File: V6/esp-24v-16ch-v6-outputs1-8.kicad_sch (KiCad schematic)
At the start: 5 parts, among them Q4 MMBT2222A

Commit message: V6 is up
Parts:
- R89: renamed from R88; Package 0402/1005 -> (none)
- R90: renamed from R89; value 1k -> 470R; LCSC Part # C11702 -> C25117; Mfr PN 0402WGF1001TCE -> 0402WGF4700TCE; Vendor PN C11702 -> C25117
- renumbered D57 to D58, R90 to R91
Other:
- note added: "I_{BASE} = (3.3V - V_{BE}) / 470R I_{BASE} = (3.3V - 0.7V) / 470R I_{BASE} = 5,53 mA ADEQUATE FOR FULL SATURATION OF THE TRANSISTOR UP TO I_{C} AROUND 550 mA CONSIDERING A FORCED BETA OF 10."

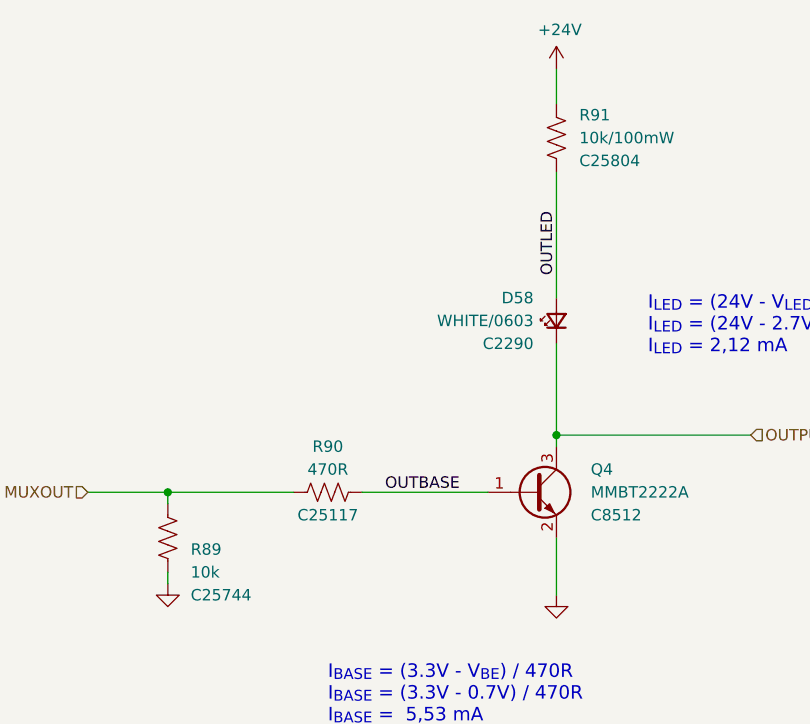
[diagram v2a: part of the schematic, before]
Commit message: Added voltage monitors for both ESP32 and LAN8710A
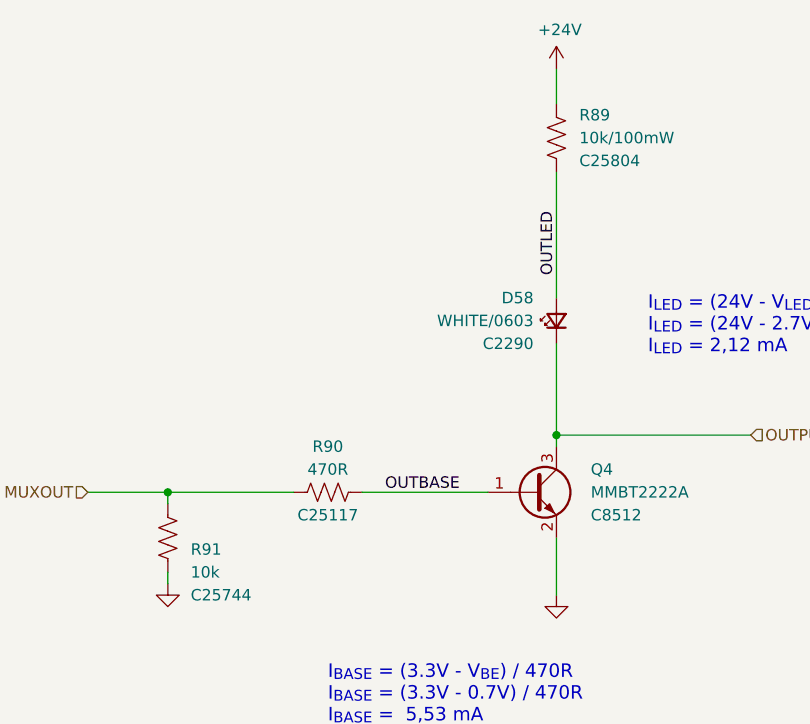
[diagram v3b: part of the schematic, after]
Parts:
- renumbered R91 to R89, R89 to R91
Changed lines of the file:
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@@
 		(title "ESP 24V 16xIn/16xOut/1-Wire Module")
 		(date "2026-02-10")
-		(rev "V6.0")
+		(rev "V6.0.3")
 	)
 	(text "I_{LED} = (24V - V_{LED} - V_{CE}) / 10k\nI_{LED} = (24V - 2.7V - 0,1V) / 10k\nI_{LED} = 2,12 mA"
@@
 		(in_pos_files yes)
 		(dnp no)
-		(property "Reference" "#PWR0217"
+		(property "Reference" "#PWR0215"
 			(at 144.78 58.42 0)
 			(hide yes)
@@
 			(project "esp-24v-16ch-v6"
 				(path "/2bc5a21a-1d79-419d-a592-6852cc07b00a/032d24f7-dea6-43c8-b36e-6c84d69a3256"
-					(reference "#PWR0232")
+					(reference "#PWR0230")
 					(unit 1)
 				)
 				(path "/2bc5a21a-1d79-419d-a592-6852cc07b00a/3a243df8-db7d-4641-87d2-b8850c504ddf"
-					(reference "#PWR0223")
+					(reference "#PWR0221")
 					(unit 1)
 				)
 				(path "/2bc5a21a-1d79-419d-a592-6852cc07b00a/471d35a0-0cf0-47e4-a6a8-e70e1f2b0cfb"
-					(reference "#PWR0226")
+					(reference "#PWR0224")
 					(unit 1)
 				)
 				(path "/2bc5a21a-1d79-419d-a592-6852cc07b00a/7e58906f-db1c-4ecb-8d31-ce9f4ea8e299"
-					(reference "#PWR0220")
+					(reference "#PWR0218")
 					(unit 1)
 				)
 				(path "/2bc5a21a-1d79-419d-a592-6852cc07b00a/946b081e-f05c-4bcc-8c7e-32876d800f86"
-					(reference "#PWR0229")
+					(reference "#PWR0227")
 					(unit 1)
 				)
 				(path "/2bc5a21a-1d79-419d-a592-6852cc07b00a/9735d90e-9107-44ae-97cf-e90e1d690a19"
-					(reference "#PWR0235")
+					(reference "#PWR0233")
 					(unit 1)
 				)
 				(path "/2bc5a21a-1d79-419d-a592-6852cc07b00a/f18c37e2-98aa-4f90-9189-e898a62cdeb8"
-					(reference "#PWR0238")
+					(reference "#PWR0236")
 					(unit 1)
 				)
 				(path "/2bc5a21a-1d79-419d-a592-6852cc07b00a/f859c883-9d79-4035-b255-4f20ee57230d"
-					(reference "#PWR0217")
+					(reference "#PWR0215")
 					(unit 1)
 				)
@@
 		(in_pos_files yes)
 		(dnp no)
-		(property "Reference" "R91"
+		(property "Reference" "R89"
 			(at 147.32 59.69 0)
 			(show_name no)
@@
 			(project "esp-24v-16ch-v6"
 				(path "/2bc5a21a-1d79-419d-a592-6852cc07b00a/032d24f7-dea6-43c8-b36e-6c84d69a3256"
-					(reference "R106")
+					(reference "R104")
 					(unit 1)
 				)
 				(path "/2bc5a21a-1d79-419d-a592-6852cc07b00a/3a243df8-db7d-4641-87d2-b8850c504ddf"
-					(reference "R97")
+					(reference "R95")
 					(unit 1)
 				)
 				(path "/2bc5a21a-1d79-419d-a592-6852cc07b00a/471d35a0-0cf0-47e4-a6a8-e70e1f2b0cfb"
-					(reference "R100")
+					(reference "R98")
 					(unit 1)
 				)
 				(path "/2bc5a21a-1d79-419d-a592-6852cc07b00a/7e58906f-db1c-4ecb-8d31-ce9f4ea8e299"
-					(reference "R94")
+					(reference "R92")
 					(unit 1)
 				)
 				(path "/2bc5a21a-1d79-419d-a592-6852cc07b00a/946b081e-f05c-4bcc-8c7e-32876d800f86"
-					(reference "R103")
+					(reference "R101")
 					(unit 1)
 				)
 				(path "/2bc5a21a-1d79-419d-a592-6852cc07b00a/9735d90e-9107-44ae-97cf-e90e1d690a19"
-					(reference "R109")
+					(reference "R107")
 					(unit 1)
 				)
 				(path "/2bc5a21a-1d79-419d-a592-6852cc07b00a/f18c37e2-98aa-4f90-9189-e898a62cdeb8"
-					(reference "R112")
+					(reference "R110")
 					(unit 1)
 				)
 				(path "/2bc5a21a-1d79-419d-a592-6852cc07b00a/f859c883-9d79-4035-b255-4f20ee57230d"
-					(reference "R91")
+					(reference "R89")
 					(unit 1)
 				)
@@
 		(in_pos_files yes)
 		(dnp no)
-		(property "Reference" "R89"
+		(property "Reference" "R91"
 			(at 104.14 107.95 0)
 			(show_name no)
@@
 			(project "esp-24v-16ch-v6"
 				(path "/2bc5a21a-1d79-419d-a592-6852cc07b00a/032d24f7-dea6-43c8-b36e-6c84d69a3256"
-					(reference "R104")
+					(reference "R106")
 					(unit 1)
 				)
 				(path "/2bc5a21a-1d79-419d-a592-6852cc07b00a/3a243df8-db7d-4641-87d2-b8850c504ddf"
-					(reference "R95")
+					(reference "R97")
 					(unit 1)
 				)
 				(path "/2bc5a21a-1d79-419d-a592-6852cc07b00a/471d35a0-0cf0-47e4-a6a8-e70e1f2b0cfb"
-					(reference "R98")
+					(reference "R100")
 					(unit 1)
 				)
 				(path "/2bc5a21a-1d79-419d-a592-6852cc07b00a/7e58906f-db1c-4ecb-8d31-ce9f4ea8e299"
-					(reference "R92")
+					(reference "R94")
 					(unit 1)
 				)
 				(path "/2bc5a21a-1d79-419d-a592-6852cc07b00a/946b081e-f05c-4bcc-8c7e-32876d800f86"
-					(reference "R101")
+					(reference "R103")
 					(unit 1)
 				)
 				(path "/2bc5a21a-1d79-419d-a592-6852cc07b00a/9735d90e-9107-44ae-97cf-e90e1d690a19"
-					(reference "R107")
+					(reference "R109")
 					(unit 1)
 				)
 				(path "/2bc5a21a-1d79-419d-a592-6852cc07b00a/f18c37e2-98aa-4f90-9189-e898a62cdeb8"
-					(reference "R110")
+					(reference "R112")
 					(unit 1)
 				)
 				(path "/2bc5a21a-1d79-419d-a592-6852cc07b00a/f859c883-9d79-4035-b255-4f20ee57230d"
-					(reference "R89")
+					(reference "R91")
 					(unit 1)
 				)
@@
 		(in_pos_files yes)
 		(dnp no)
-		(property "Reference" "#PWR0218"
+		(property "Reference" "#PWR0217"
 			(at 144.78 119.38 0)
 			(hide yes)
@@
 			(project "esp-24v-16ch-v6"
 				(path "/2bc5a21a-1d79-419d-a592-6852cc07b00a/032d24f7-dea6-43c8-b36e-6c84d69a3256"
-					(reference "#PWR0233")
+					(reference "#PWR0232")
 					(unit 1)
 				)
 				(path "/2bc5a21a-1d79-419d-a592-6852cc07b00a/3a243df8-db7d-4641-87d2-b8850c504ddf"
-					(reference "#PWR0224")
+					(reference "#PWR0223")
 					(unit 1)
 				)
 				(path "/2bc5a21a-1d79-419d-a592-6852cc07b00a/471d35a0-0cf0-47e4-a6a8-e70e1f2b0cfb"
-					(reference "#PWR0227")
+					(reference "#PWR0226")
 					(unit 1)
 				)
 				(path "/2bc5a21a-1d79-419d-a592-6852cc07b00a/7e58906f-db1c-4ecb-8d31-ce9f4ea8e299"
-					(reference "#PWR0221")
+					(reference "#PWR0220")
 					(unit 1)
 				)
 				(path "/2bc5a21a-1d79-419d-a592-6852cc07b00a/946b081e-f05c-4bcc-8c7e-32876d800f86"
-					(reference "#PWR0230")
+					(reference "#PWR0229")
 					(unit 1)
 				)
 				(path "/2bc5a21a-1d79-419d-a592-6852cc07b00a/9735d90e-9107-44ae-97cf-e90e1d690a19"
-					(reference "#PWR0236")
+					(reference "#PWR0235")
 					(unit 1)
 				)
 				(path "/2bc5a21a-1d79-419d-a592-6852cc07b00a/f18c37e2-98aa-4f90-9189-e898a62cdeb8"
-					(reference "#PWR0239")
+					(reference "#PWR0238")
 					(unit 1)
 				)
 				(path "/2bc5a21a-1d79-419d-a592-6852cc07b00a/f859c883-9d79-4035-b255-4f20ee57230d"
-					(reference "#PWR0218")
-					(unit 1)
-				)
+					(reference "#PWR0217")
+					(unit 1)
+				)
